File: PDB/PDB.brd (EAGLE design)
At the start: 160 x 101.6 mm, 57 parts, among them Q1 IRFML8244, Q2 IRFML8244, Q3 PMOSFET, Q4 P-CHANNEL-MOSFETSOT23-3, Q5 P-CHANNEL-MOSFETSOT23-3

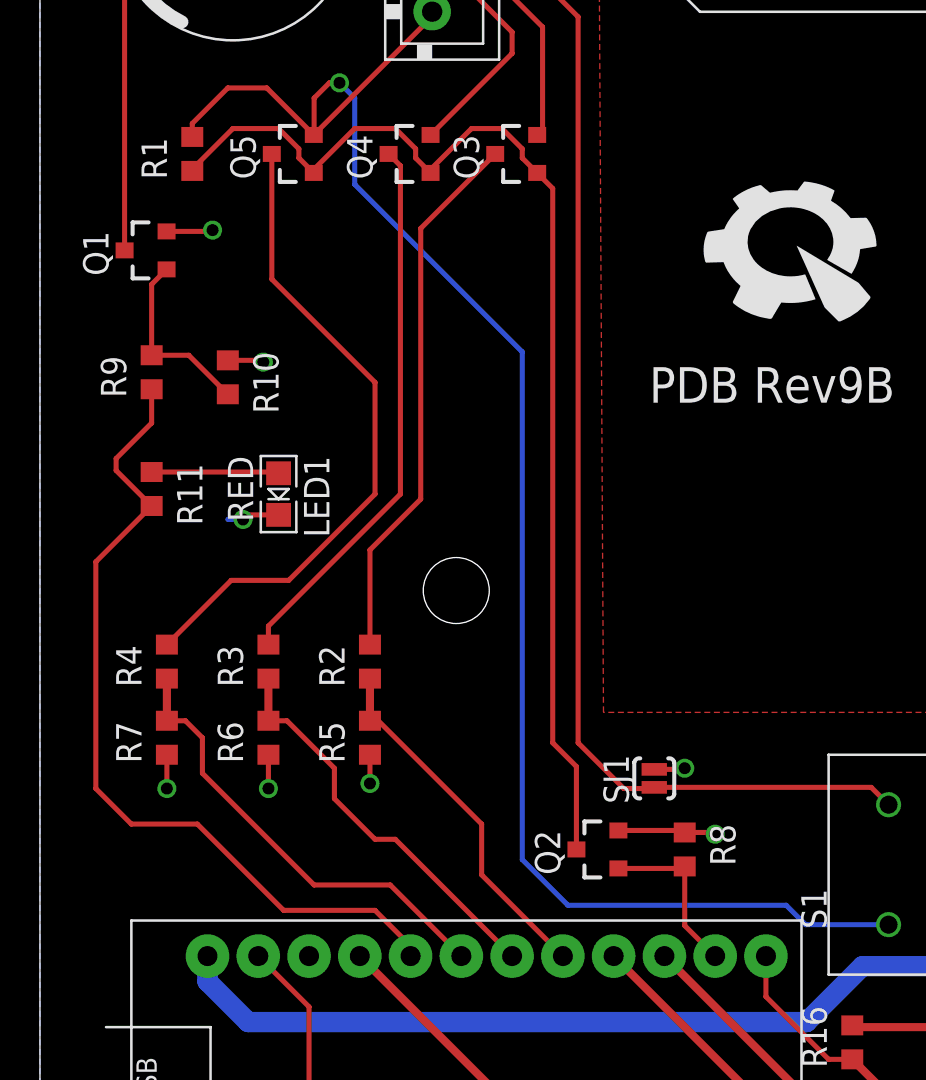
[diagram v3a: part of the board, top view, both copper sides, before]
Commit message: Fix silk screen conflicts and add cam job
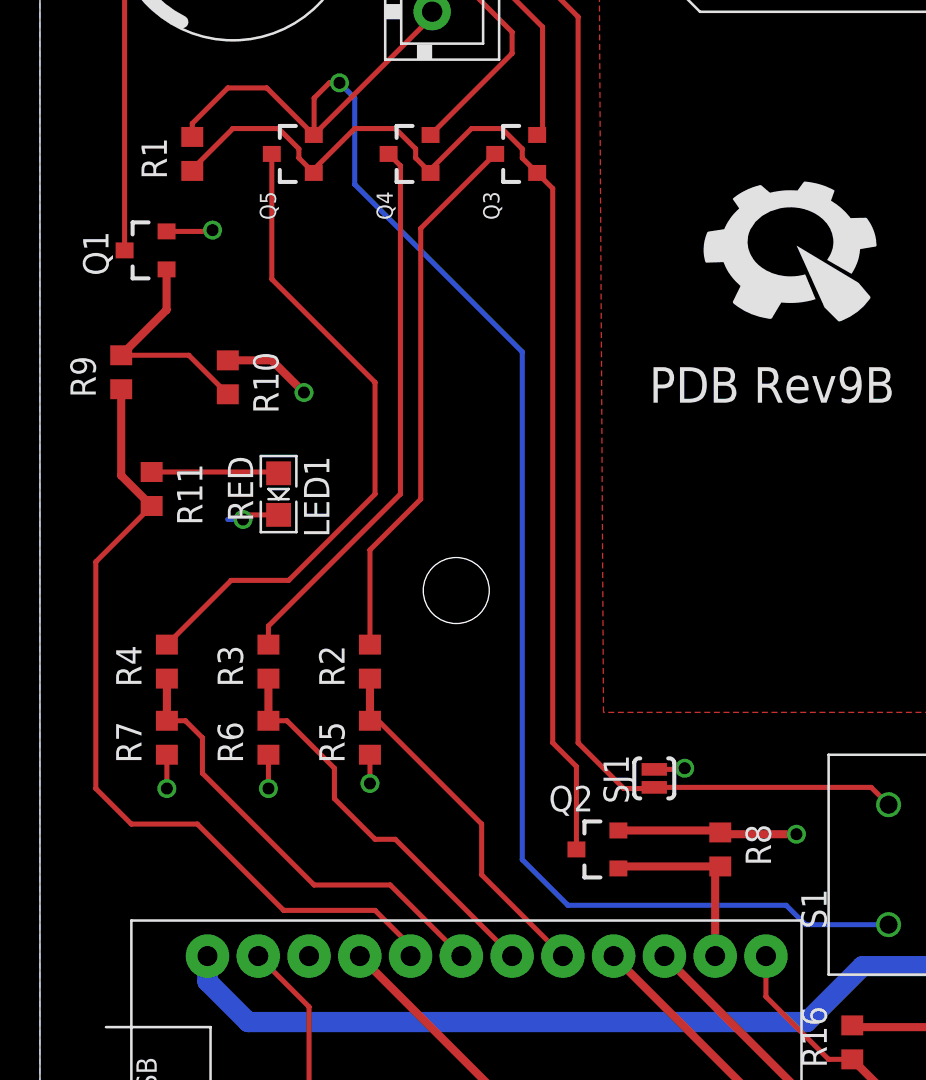
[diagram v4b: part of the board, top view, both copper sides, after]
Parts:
- moved R8 1.78 mm to (34.0, 47.8)
- moved R9 1.52 mm to (4.06, 71.6)
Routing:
- net GND: track 137.3 -> 144.0 mm
- net N$6: track 9.22 -> 11.4 mm
- net DIV_EN: track 8.47 -> 9.73 mm
- net BUZZER_SIGNAL: track 42.1 -> 41.3 mm
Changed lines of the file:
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@@
 <attribute name="PIE_DIGIKEY-PN" value="102-1269-ND" x="-20.828" y="127.254" size="1.778" layer="27" rot="R270" display="off"/>
 </element>
-<element name="R9" library="pie" package="R0603" value="100" x="5.588" y="71.628" rot="R90">
-<attribute name="PIE-INT-REF-NUM" value="RESISTOR-GENERIC" x="-18.542" y="27.178" size="1.778" layer="27" rot="R90" display="off"/>
+<element name="R9" library="pie" package="R0603" value="100" x="4.064" y="71.628" rot="R90">
+<attribute name="PIE-INT-REF-NUM" value="RESISTOR-GENERIC" x="-20.066" y="27.178" size="1.778" layer="27" rot="R90" display="off"/>
 </element>
 <element name="R10" library="pie" package="R0603" value="10k" x="9.398" y="71.374" rot="R270">
@@
 <attribute name="PIE-INT-REF-NUM" value="LED" x="17.018" y="103.632" size="1.778" layer="27" rot="R270" display="off"/>
 </element>
-<element name="Q5" library="pie" package="SOT23-3" value="P-CHANNEL-MOSFETSOT23-3" x="12.7" y="82.55" rot="R90">
+<element name="Q5" library="pie" package="SOT23-3" value="P-CHANNEL-MOSFETSOT23-3" x="12.7" y="82.55" smashed="yes" rot="R90">
 <attribute name="PIE-DIGIKEY-PN-PRI" value="IRLML6402PBFCT-ND" x="22.86" y="69.85" size="1.778" layer="27" rot="R90" display="off"/>
 <attribute name="PIE-INT-REF-NUM" value="PMOS" x="22.86" y="69.85" size="1.778" layer="27" rot="R90" display="off"/>
-</element>
-<element name="Q4" library="pie" package="SOT23-3" value="P-CHANNEL-MOSFETSOT23-3" x="18.542" y="82.55" rot="R90">
+<attribute name="NAME" x="11.811" y="79.248" size="0.8128" layer="25" font="vector" ratio="10" rot="R90"/>
+<attribute name="VALUE" x="15.367" y="67.31" size="0.8128" layer="27" font="vector" rot="R90"/>
+</element>
+<element name="Q4" library="pie" package="SOT23-3" value="P-CHANNEL-MOSFETSOT23-3" x="18.542" y="82.55" smashed="yes" rot="R90">
 <attribute name="PIE-DIGIKEY-PN-PRI" value="IRLML6402PBFCT-ND" x="50.292" y="44.45" size="1.778" layer="27" rot="R90" display="off"/>
 <attribute name="PIE-INT-REF-NUM" value="PMOS" x="50.292" y="44.45" size="1.778" layer="27" rot="R90" display="off"/>
-</element>
-<element name="Q3" library="pie" package="SOT23-3" value="PMOSFET" x="23.876" y="82.55" rot="R90">
+<attribute name="NAME" x="17.653" y="79.248" size="0.8128" layer="25" font="vector" ratio="10" rot="R90"/>
+<attribute name="VALUE" x="21.209" y="67.31" size="0.8128" layer="27" font="vector" rot="R90"/>
+</element>
+<element name="Q3" library="pie" package="SOT23-3" value="PMOSFET" x="23.876" y="82.55" smashed="yes" rot="R90">
 <attribute name="PIE-DIGIKEY-PN-PRI" value="IRLML6402PBFCT-ND" x="41.656" y="69.85" size="1.778" layer="27" rot="R90" display="off"/>
 <attribute name="PIE-INT-REF-NUM" value="PMOS" x="41.656" y="69.85" size="1.778" layer="27" rot="R90" display="off"/>
-</element>
-<element name="Q2" library="pie" package="SOT23-3" value="IRFML8244" x="27.94" y="47.752" rot="R90"/>
+<attribute name="NAME" x="22.987" y="79.248" size="0.8128" layer="25" font="vector" ratio="10" rot="R90"/>
+<attribute name="VALUE" x="26.543" y="79.248" size="0.8128" layer="27" font="vector" rot="R90"/>
+</element>
+<element name="Q2" library="pie" package="SOT23-3" value="IRFML8244" x="27.94" y="47.752" smashed="yes" rot="R90">
+<attribute name="NAME" x="27.686" y="50.927" size="1.27" layer="25" font="vector" ratio="10" rot="R180"/>
+<attribute name="VALUE" x="30.734" y="45.847" size="1.27" layer="27" font="vector" rot="R180"/>
+</element>
 <element name="R1" library="pie" package="R0603" value="10k" x="7.62" y="82.55" rot="R90">
 <attribute name="PIE-INT-REF-NUM" value="RESISTOR-GENERIC" x="33.02" y="53.34" size="1.778" layer="27" rot="R90" display="off"/>
 </element>
-<element name="R8" library="pie" package="R0603" value="10k" x="32.258" y="47.752" rot="R270">
-<attribute name="PIE-INT-REF-NUM" value="RESISTOR-GENERIC" x="0.508" y="112.522" size="1.778" layer="27" rot="R270" display="off"/>
+<element name="R8" library="pie" package="R0603" value="10k" x="34.036" y="47.752" rot="R270">
+<attribute name="PIE-INT-REF-NUM" value="RESISTOR-GENERIC" x="2.286" y="112.522" size="1.778" layer="27" rot="R270" display="off"/>
 </element>
 <element name="Q1" library="pie" package="SOT23-3" value="IRFML8244" x="5.334" y="77.724" rot="R90"/>
@@
 <wire x1="8.57" y1="78.674" x2="8.636" y2="78.74" width="0.254" layer="1"/>
 <via x="8.636" y="78.74" extent="1-16" drill="0.6"/>
-<wire x1="9.398" y1="72.224" x2="11.088" y2="72.224" width="0.254" layer="1"/>
-<wire x1="11.088" y1="72.224" x2="11.176" y2="72.136" width="0.254" layer="1"/>
-<via x="11.176" y="72.136" extent="1-16" drill="0.6"/>
+<via x="13.208" y="70.612" extent="1-16" drill="0.6"/>
 <wire x1="11.938" y1="64.4906" x2="10.3886" y2="64.4906" width="0.254" layer="1"/>
 <wire x1="10.3886" y1="64.4906" x2="10.16" y2="64.262" width="0.254" layer="1"/>
@@
 <wire x1="32.2" y1="51.758" x2="32.258" y2="51.816" width="0.254" layer="1"/>
 <via x="32.258" y="51.816" extent="1-16" drill="0.6"/>
-<wire x1="28.94" y1="48.702" x2="32.158" y2="48.702" width="0.254" layer="1"/>
-<wire x1="32.158" y1="48.702" x2="32.258" y2="48.602" width="0.254" layer="1"/>
-<wire x1="32.258" y1="48.602" x2="33.694" y2="48.602" width="0.254" layer="1"/>
-<wire x1="33.694" y1="48.602" x2="33.782" y2="48.514" width="0.254" layer="1"/>
-<via x="33.782" y="48.514" extent="1-16" drill="0.6"/>
+<wire x1="33.936" y1="48.702" x2="34.036" y2="48.602" width="0.254" layer="1"/>
+<via x="37.846" y="48.514" extent="1-16" drill="0.6"/>
 <wire x1="45.72" y1="2.794" x2="54.737" y2="2.794" width="0.4064" layer="1"/>
 <wire x1="54.737" y1="2.794" x2="57.023" y2="5.08" width="0.4064" layer="1"/>
@@
 <wire x1="47.244" y1="38.862" x2="40.728" y2="38.862" width="0.4064" layer="1"/>
 <wire x1="40.728" y1="38.862" x2="40.64" y2="38.95" width="0.4064" layer="1"/>
+<wire x1="9.398" y1="72.224" x2="11.596" y2="72.224" width="0.4064" layer="1"/>
+<wire x1="11.596" y1="72.224" x2="13.208" y2="70.612" width="0.4064" layer="1"/>
+<wire x1="34.036" y1="48.602" x2="34.124" y2="48.514" width="0.4064" layer="1"/>
+<wire x1="34.124" y1="48.514" x2="37.846" y2="48.514" width="0.4064" layer="1"/>
+<wire x1="33.936" y1="48.702" x2="28.94" y2="48.702" width="0.4064" layer="1"/>
 </signal>
 <signal name="VOUT2">
@@
 <contactref element="R10" pad="2"/>
 <contactref element="Q1" pad="1"/>
-<wire x1="5.588" y1="72.478" x2="5.588" y2="76.028" width="0.254" layer="1"/>
-<wire x1="5.588" y1="76.028" x2="6.334" y2="76.774" width="0.254" layer="1"/>
-<wire x1="5.588" y1="72.478" x2="7.444" y2="72.478" width="0.254" layer="1"/>
+<wire x1="4.064" y1="72.478" x2="7.444" y2="72.478" width="0.254" layer="1"/>
 <wire x1="7.444" y1="72.478" x2="9.398" y2="70.524" width="0.254" layer="1"/>
+<wire x1="4.064" y1="72.478" x2="6.334" y2="74.748" width="0.4064" layer="1"/>
+<wire x1="6.334" y1="74.748" x2="6.334" y2="76.774" width="0.4064" layer="1"/>
 </signal>
 <signal name="N$5">
@@
 <contactref element="R11" pad="2"/>
 <contactref element="UC1" pad="A3"/>
-<wire x1="5.588" y1="70.778" x2="5.588" y2="69.088" width="0.254" layer="1"/>
-<wire x1="5.588" y1="69.088" x2="3.81" y2="67.31" width="0.254" layer="1"/>
-<wire x1="3.81" y1="67.31" x2="3.81" y2="66.714" width="0.254" layer="1"/>
-<wire x1="3.81" y1="66.714" x2="5.588" y2="64.936" width="0.254" layer="1"/>
 <wire x1="18.542" y1="42.418" x2="18.542" y2="42.926" width="0.254" layer="1"/>
 <wire x1="18.542" y1="42.926" x2="16.764" y2="44.704" width="0.254" layer="1"/>
@@
 <wire x1="2.794" y1="50.8" x2="2.794" y2="62.142" width="0.254" layer="1"/>
 <wire x1="2.794" y1="62.142" x2="5.588" y2="64.936" width="0.254" layer="1"/>
+<wire x1="5.588" y1="64.936" x2="4.064" y2="66.46" width="0.4064" layer="1"/>
+<wire x1="4.064" y1="66.46" x2="4.064" y2="70.778" width="0.4064" layer="1"/>
 </signal>
 <signal name="N$1">
@@
 <contactref element="R8" pad="2"/>
 <contactref element="UC1" pad="16"/>
-<wire x1="28.94" y1="46.802" x2="32.158" y2="46.802" width="0.254" layer="1"/>
-<wire x1="32.158" y1="46.802" x2="32.258" y2="46.902" width="0.254" layer="1"/>
-<wire x1="32.258" y1="46.902" x2="32.258" y2="43.942" width="0.254" layer="1"/>
-<wire x1="32.258" y1="43.942" x2="33.782" y2="42.418" width="0.254" layer="1"/>
+<wire x1="28.94" y1="46.802" x2="29.04" y2="46.902" width="0.4064" layer="1"/>
+<wire x1="29.04" y1="46.902" x2="34.036" y2="46.902" width="0.4064" layer="1"/>
+<wire x1="34.036" y1="46.902" x2="33.782" y2="46.648" width="0.4064" layer="1"/>
+<wire x1="33.782" y1="46.648" x2="33.782" y2="42.418" width="0.4064" layer="1"/>
 </signal>
 <signal name="N$2">

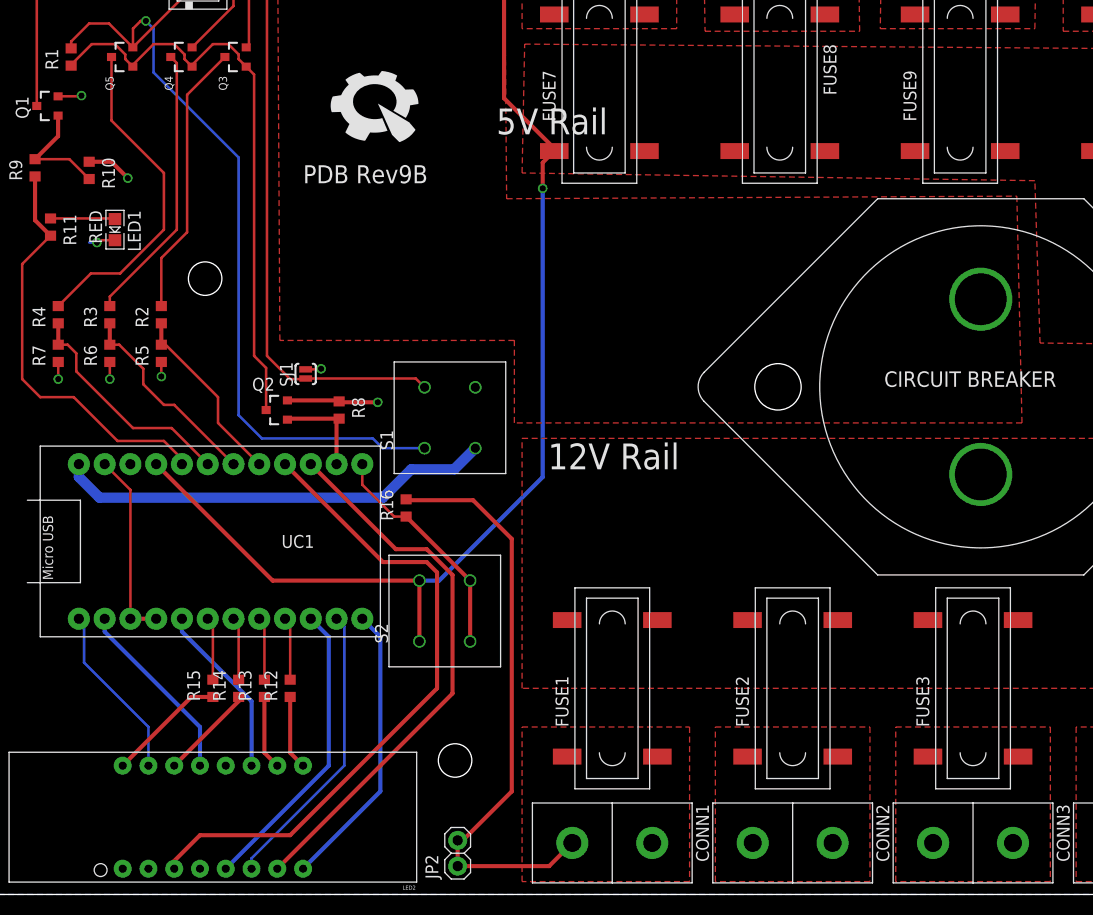
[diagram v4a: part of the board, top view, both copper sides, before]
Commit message: Fix CIRC_BREAKER pckg offset; change name/val size for DPDT_SW and MOSFETs; update all parts to SS/pie.lbr
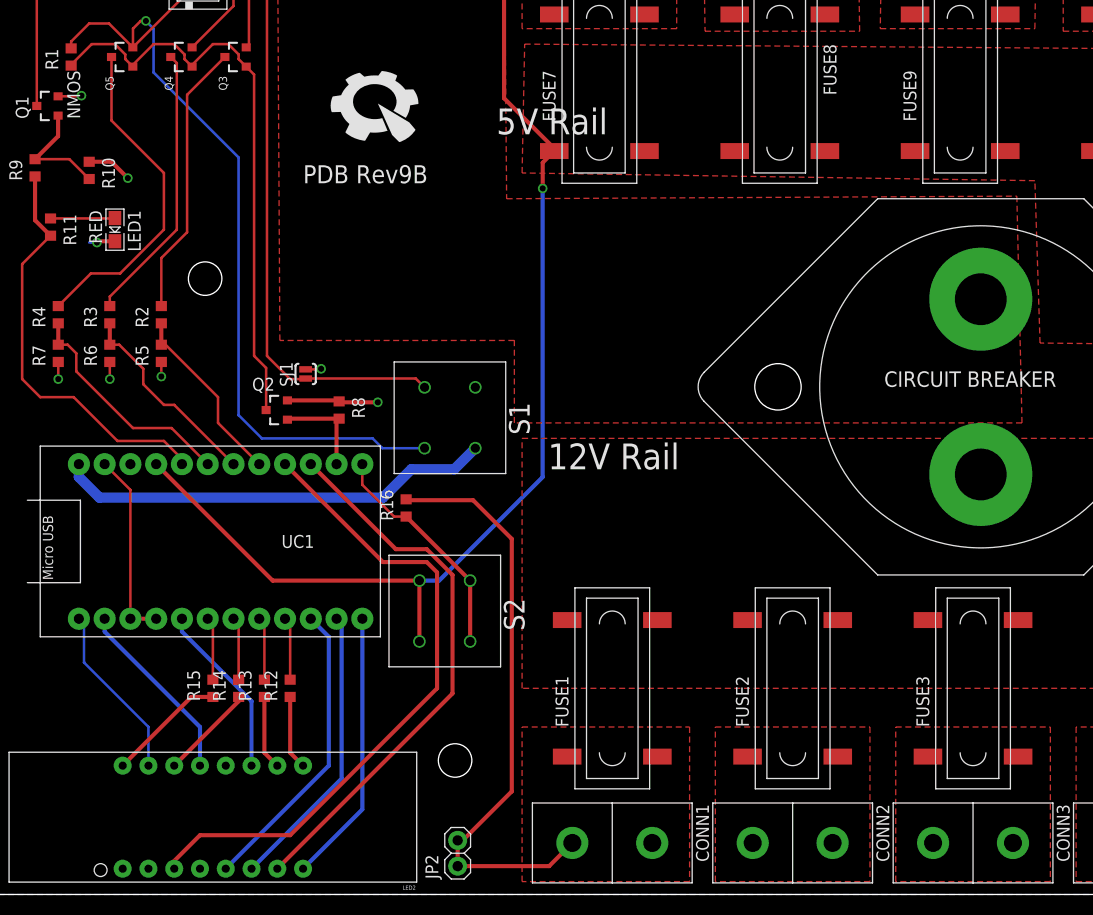
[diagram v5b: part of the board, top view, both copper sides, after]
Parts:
- Q1: value IRFML8244 -> NMOS
- Q3: value PMOSFET -> PMOS
- Q4, Q5: value P-CHANNEL-MOSFETSOT23-3 -> PMOS
- R1, R10, R16, R2, R5, R6, R7, R8: value 10k -> >VALUE
- R11: value 130 -> >VALUE
- R12, R13, R14, R15: value 330 -> >VALUE
- R3: value 30k -> >VALUE
- R4: value 51k -> >VALUE
- R9: value 100 -> >VALUE
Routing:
- net B: track 28.5 -> 27.1 mm

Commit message: Add back resistor values for battery buzzer
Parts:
- R1, R10, R16, R2, R5, R6, R7, R8: value >VALUE -> 10k
- R11: value >VALUE -> 130
- R12, R13, R14, R15: value >VALUE -> 330
- R3: value >VALUE -> 30k
- R4: value >VALUE -> 51k
- R9: value >VALUE -> 100
